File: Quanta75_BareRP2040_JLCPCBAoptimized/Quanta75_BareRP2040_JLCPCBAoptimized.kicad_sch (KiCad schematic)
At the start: 249 parts, among them J1 USB_C_Receptacle_USB2.0, J10 Conn_01x05_Socket GPIOs, J2 Conn_01x02_Socket VBUS 5V, J3 Conn_01x02_Socket 3V3, J5 Conn_01x04_Socket SWD, J6 USB_A_Receptacle_UBS2.0, J7 USB_C_Receptacle_USB2.0, J8 Conn_01x04_Socket I2C display, J9 USB_C_Receptacle_USB2.0, SW1 SW_Push, SW10 SW_Push, SW11 SW_Push, SW12 SW_Push, SW13 SW_Push, SW14 SW_Push, SW15 SW_Push, SW16 SW_Push, SW17 SW_Push, SW18 SW_Push, SW19 SW_Push, SW2 SW_Push, SW20 SW_Push, SW21 SW_Push, SW22 SW_Push, SW23 SW_Push, SW24 SW_Push, SW25 SW_Push, SW26 SW_Push, SW27 SW_Push, SW28 SW_Push, SW29 SW_Push, SW3 SW_Push, SW30 SW_Push, SW31 SW_Push, SW32 SW_Push, SW33 SW_Push, SW34 SW_Push, SW35 SW_Push, SW36 SW_Push, SW37 SW_Push, SW38 SW_Push, SW39 SW_Push, SW4 SW_Push, SW40 SW_Push, SW41 SW_Push, SW42 SW_Push, SW43 SW_Push, SW44 SW_Push, SW45 SW_Push, SW46 SW_Push, SW47 SW_Push, SW48 SW_Push, SW49 SW_Push, SW5 SW_Push, SW50 SW_Push, SW51 SW_Push, SW52 SW_Push, SW53 SW_Push, SW54 SW_Push, SW55 SW_Push, SW56 SW_Push, SW57 SW_Push, SW58 SW_Push, SW59 SW_Push, SW6 SW_Push, SW60 SW_Push, SW61 SW_Push, SW62 SW_Push, SW63 SW_Push, SW64 SW_Push, SW65 SW_Push, SW66 SW_Push, SW67 SW_Push, SW68 SW_Push, SW69 SW_Push, SW7 SW_Push, SW70 SW_Push, SW71 SW_Push, SW72 SW_Push, SW73 SW_Push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

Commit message: update pcb
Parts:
- removed D88: Amber LED, LED_THT:LED_D3.0mm_Clear, symbol Device:LED
- C12: footprint Resistor_SMD:R_0805_2012Metric_Pad1.20x1.40mm_HandSolder -> Capacitor_SMD:C_0805_2012Metric_Pad1.18x1.45mm_HandSolder
- C13, C14, C16, C17, C18, C19, C20, C21, C22: footprint Resistor_SMD:R_0603_1608Metric_Pad0.98x0.95mm_HandSolder -> Capacitor_SMD:C_0603_1608Metric_Pad1.08x0.95mm_HandSolder
- C25, C26: footprint Resistor_SMD:R_0402_1005Metric_Pad0.72x0.64mm_HandSolder -> Capacitor_SMD:C_0402_1005Metric_Pad0.74x0.62mm_HandSolder
- U1: footprint Package_DFN_QFN:QFN-56-1EP_7x7mm_P0.4mm_EP3.2x3.2mm -> Package_DFN_QFN:QFN-56-1EP_7x7mm_P0.4mm_EP3.2x3.2mm_ThermalVias
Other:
- moved on the sheet: D87
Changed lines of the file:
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@@
   (junction (at 254 101.6) (diameter 0) (color 0 0 0 0)
   )
-  (junction (at 405.13 364.49) (diameter 0) (color 0 0 0 0)
-  )
   (junction (at 87.63 309.88) (diameter 0) (color 0 0 0 0)
   )
@@
   (junction (at 171.45 101.6) (diameter 0) (color 0 0 0 0)
   )
-  (junction (at 400.05 353.06) (diameter 0) (color 0 0 0 0)
-  )
   (junction (at 204.47 170.18) (diameter 0) (color 0 0 0 0)
   )
@@
     (stroke (width 0) (type default))
   )
-  (wire (pts (xy 394.97 364.49) (xy 405.13 364.49))
+  (wire (pts (xy 400.05 364.49) (xy 407.67 364.49))
     (stroke (width 0) (type default))
   )
@@
     (stroke (width 0) (type default))
   )
-  (wire (pts (xy 394.97 353.06) (xy 400.05 353.06))
-    (stroke (width 0) (type default))
-  )
   (wire (pts (xy 99.06 144.78) (xy 99.06 147.32))
     (stroke (width 0) (type default))
@@
     (stroke (width 0) (type default))
   )
-  (wire (pts (xy 407.67 364.49) (xy 405.13 364.49))
-    (stroke (width 0) (type default))
-  )
   (wire (pts (xy 427.99 105.41) (xy 433.07 105.41))
     (stroke (width 0) (type default))
@@
     (stroke (width 0) (type default))
   )
-  (wire (pts (xy 394.97 364.49) (xy 394.97 361.95))
+  (wire (pts (xy 400.05 364.49) (xy 400.05 359.41))
     (stroke (width 0) (type default))
   )
@@
     (stroke (width 0) (type default))
   )
-  (wire (pts (xy 405.13 364.49) (xy 405.13 361.95))
-    (stroke (width 0) (type default))
-  )
   (wire (pts (xy 198.12 109.22) (xy 214.63 109.22))
     (stroke (width 0) (type default))
@@
     (stroke (width 0) (type default))
   )
-  (wire (pts (xy 394.97 353.06) (xy 394.97 354.33))
+  (wire (pts (xy 400.05 346.71) (xy 400.05 351.79))
     (stroke (width 0) (type default))
   )
@@
     (stroke (width 0) (type default))
   )
-  (wire (pts (xy 405.13 354.33) (xy 405.13 353.06))
-    (stroke (width 0) (type default))
-  )
   (wire (pts (xy 505.46 181.61) (xy 519.43 181.61))
     (stroke (width 0) (type default))
@@
     (stroke (width 0) (type default))
   )
-  (wire (pts (xy 400.05 346.71) (xy 400.05 353.06))
-    (stroke (width 0) (type default))
-  )
   (wire (pts (xy 115.57 86.36) (xy 115.57 88.9))
     (stroke (width 0) (type default))
@@
     (stroke (width 0) (type default))
   )
-  (wire (pts (xy 400.05 353.06) (xy 405.13 353.06))
-    (stroke (width 0) (type default))
-  )
   (wire (pts (xy 198.12 40.64) (xy 214.63 40.64))
     (stroke (width 0) (type default))
@@
       (effects (font (size 1.27 1.27)) (justify left))
     )
-    (property "Footprint" "Package_DFN_QFN:QFN-56-1EP_7x7mm_P0.4mm_EP3.2x3.2mm" (at 153.67 381 0)
+    (property "Footprint" "Package_DFN_QFN:QFN-56-1EP_7x7mm_P0.4mm_EP3.2x3.2mm_ThermalVias" (at 153.67 381 0)
       (effects (font (size 1.27 1.27)) hide)
     )
@@
       (effects (font (size 1.27 1.27)) (justify left))
     )
-    (property "Footprint" "Resistor_SMD:R_0603_1608Metric_Pad0.98x0.95mm_HandSolder" (at 187.96 246.38 0)
+    (property "Footprint" "Capacitor_SMD:C_0603_1608Metric_Pad1.08x0.95mm_HandSolder" (at 187.96 246.38 0)
       (effects (font (size 1.27 1.27)) hide)
     )
@@
       (effects (font (size 1.27 1.27)) (justify left))
     )
-    (property "Footprint" "Resistor_SMD:R_0603_1608Metric_Pad0.98x0.95mm_HandSolder" (at 172.72 246.38 0)
+    (property "Footprint" "Capacitor_SMD:C_0603_1608Metric_Pad1.08x0.95mm_HandSolder" (at 172.72 246.38 0)
       (effects (font (size 1.27 1.27)) hide)
     )
@@
     )
   )
-  (symbol (lib_id "Device:LED") (at 405.13 358.14 90) (unit 1)
-    (in_bom no) (on_board yes) (dnp yes)
-    (property "Reference" "D88" (at 401.32 359.41 0)
-      (effects (font (size 1.27 1.27)))
-    )
-    (property "Value" "Amber LED" (at 402.9192 358.9145 0)
-      (effects (font (size 1.27 1.27)))
-    )
-    (property "Footprint" "LED_THT:LED_D3.0mm_Clear" (at 405.13 358.14 0)
-      (effects (font (size 1.27 1.27)) hide)
-    )
-    (property "Datasheet" "~" (at 405.13 358.14 0)
-      (effects (font (size 1.27 1.27)) hide)
-    )
-    (pin "1")
-    (pin "2")
-    (instances
-      (project "Quanta75_BareRP2040_JLCPCBAoptimized"
-        (path "/0cabb2e6-4a46-4ffe-8ff7-d51fc1f6dda5"
-          (reference "D88") (unit 1)
-        )
-      )
-    )
-  )
   (symbol (lib_id "pspice:DIODE") (at 77.47 55.88 0) (unit 1)
     (in_bom yes) (on_board yes) (dnp no)
@@
       (effects (font (size 1.27 1.27)) (justify left))
     )
-    (property "Footprint" "Resistor_SMD:R_0402_1005Metric_Pad0.72x0.64mm_HandSolder" (at 135.89 261.62 0)
+    (property "Footprint" "Capacitor_SMD:C_0402_1005Metric_Pad0.74x0.62mm_HandSolder" (at 135.89 261.62 0)
       (effects (font (size 1.27 1.27)) hide)
     )
@@
       (effects (font (size 1.27 1.27)) (justify left))
     )
-    (property "Footprint" "Resistor_SMD:R_0603_1608Metric_Pad0.98x0.95mm_HandSolder" (at 110.49 246.38 0)
+    (property "Footprint" "Capacitor_SMD:C_0603_1608Metric_Pad1.08x0.95mm_HandSolder" (at 110.49 246.38 0)
       (effects (font (size 1.27 1.27)) hide)
     )
@@
       (effects (font (size 1.27 1.27)) (justify left))
     )
-    (property "Footprint" "Resistor_SMD:R_0603_1608Metric_Pad0.98x0.95mm_HandSolder" (at 69.85 248.92 0)
+    (property "Footprint" "Capacitor_SMD:C_0603_1608Metric_Pad1.08x0.95mm_HandSolder" (at 69.85 248.92 0)
       (effects (font (size 1.27 1.27)) hide)
     )
@@
       (effects (font (size 1.27 1.27)) (justify left))
     )
-    (property "Footprint" "Resistor_SMD:R_0402_1005Metric_Pad0.72x0.64mm_HandSolder" (at 149.86 261.62 0)
+    (property "Footprint" "Capacitor_SMD:C_0402_1005Metric_Pad0.74x0.62mm_HandSolder" (at 149.86 261.62 0)
       (effects (font (size 1.27 1.27)) hide)
     )
@@
       (effects (font (size 1.27 1.27)) (justify left))
     )
-    (property "Footprint" "Resistor_SMD:R_0603_1608Metric_Pad0.98x0.95mm_HandSolder" (at 120.65 246.38 0)
+    (property "Footprint" "Capacitor_SMD:C_0603_1608Metric_Pad1.08x0.95mm_HandSolder" (at 120.65 246.38 0)
       (effects (font (size 1.27 1.27)) hide)
     )
@@
       (effects (font (size 1.27 1.27)) (justify left))
     )
-    (property "Footprint" "Resistor_SMD:R_0603_1608Metric_Pad0.98x0.95mm_HandSolder" (at 165.1 246.38 0)
+    (property "Footprint" "Capacitor_SMD:C_0603_1608Metric_Pad1.08x0.95mm_HandSolder" (at 165.1 246.38 0)
       (effects (font (size 1.27 1.27)) hide)
     )
@@
     )
   )
-  (symbol (lib_id "Device:LED") (at 394.97 358.14 90) (unit 1)
+  (symbol (lib_id "Device:LED") (at 400.05 355.6 90) (unit 1)
     (in_bom no) (on_board yes) (dnp yes)
-    (property "Reference" "D87" (at 391.16 359.41 0)
+    (property "Reference" "D87" (at 396.24 356.87 0)
       (effects (font (size 1.27 1.27)))
     )
-    (property "Value" "Amber LED" (at 392.7179 359.3421 0)
+    (property "Value" "Amber LED" (at 397.7979 356.8021 0)
       (effects (font (size 1.27 1.27)))
     )
-    (property "Footprint" "LED_THT:LED_D5.0mm_Clear" (at 394.97 358.14 0)
+    (property "Footprint" "LED_THT:LED_D5.0mm_Clear" (at 400.05 355.6 0)
       (effects (font (size 1.27 1.27)) hide)
     )
-    (property "Datasheet" "~" (at 394.97 358.14 0)
+    (property "Datasheet" "~" (at 400.05 355.6 0)
       (effects (font (size 1.27 1.27)) hide)
     )
@@
       (effects (font (size 1.27 1.27)) (justify left))
     )
-    (property "Footprint" "Resistor_SMD:R_0603_1608Metric_Pad0.98x0.95mm_HandSolder" (at 195.58 246.38 0)
+    (property "Footprint" "Capacitor_SMD:C_0603_1608Metric_Pad1.08x0.95mm_HandSolder" (at 195.58 246.38 0)
       (effects (font (size 1.27 1.27)) hide)
     )
@@
       (effects (font (size 1.27 1.27)) (justify left))
     )
-    (property "Footprint" "Resistor_SMD:R_0603_1608Metric_Pad0.98x0.95mm_HandSolder" (at 180.34 246.38 0)
+    (property "Footprint" "Capacitor_SMD:C_0603_1608Metric_Pad1.08x0.95mm_HandSolder" (at 180.34 246.38 0)
       (effects (font (size 1.27 1.27)) hide)
     )
@@
       (effects (font (size 1.27 1.27)) (justify left))
     )
-    (property "Footprint" "Resistor_SMD:R_0805_2012Metric_Pad1.20x1.40mm_HandSolder" (at 81.28 248.92 0)
+    (property "Footprint" "Capacitor_SMD:C_0805_2012Metric_Pad1.18x1.45mm_HandSolder" (at 81.28 248.92 0)
       (effects (font (size 1.27 1.27)) hide)
     )
@@
       (effects (font (size 1.27 1.27)) (justify left))
     )
-    (property "Footprint" "Resistor_SMD:R_0603_1608Metric_Pad0.98x0.95mm_HandSolder" (at 49.53 248.92 0)
+    (property "Footprint" "Capacitor_SMD:C_0603_1608Metric_Pad1.08x0.95mm_HandSolder" (at 49.53 248.92 0)
       (effects (font (size 1.27 1.27)) hide)
     )

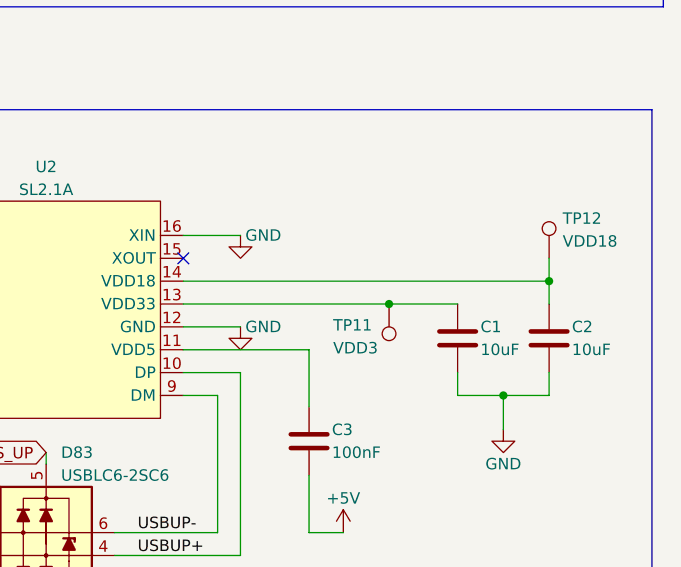
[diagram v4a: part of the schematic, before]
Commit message: finalized rp2040 version placements
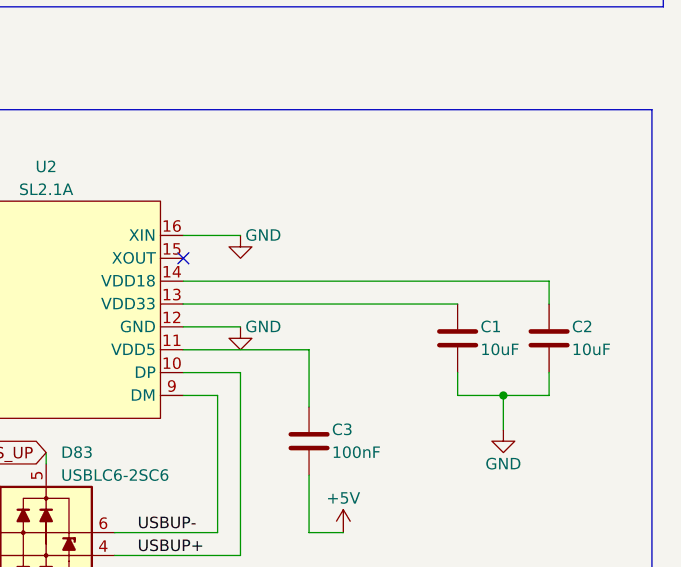
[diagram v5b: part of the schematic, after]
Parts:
- removed TP11: VDD3, TestPoint:TestPoint_Pad_D1.5mm, symbol Connector:TestPoint
- removed TP12: VDD18, TestPoint:TestPoint_Pad_D1.5mm, symbol Connector:TestPoint
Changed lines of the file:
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@@
   (junction (at 247.65 40.64) (diameter 0) (color 0 0 0 0)
   )
-  (junction (at 535.94 153.67) (diameter 0) (color 0 0 0 0)
-  )
   (junction (at 105.41 147.32) (diameter 0) (color 0 0 0 0)
   )
@@
   (junction (at 69.85 245.11) (diameter 0) (color 0 0 0 0)
   )
-  (junction (at 553.72 151.13) (diameter 0) (color 0 0 0 0)
-  )
   (junction (at 172.72 241.3) (diameter 0) (color 0 0 0 0)
   )
@@
     (stroke (width 0) (type default))
   )
-  (wire (pts (xy 543.56 153.67) (xy 535.94 153.67))
-    (stroke (width 0) (type default))
-  )
   (wire (pts (xy 237.49 78.74) (xy 237.49 101.6))
     (stroke (width 0) (type default))
@@
     (stroke (width 0) (type default))
   )
-  (wire (pts (xy 513.08 153.67) (xy 535.94 153.67))
+  (wire (pts (xy 513.08 153.67) (xy 543.56 153.67))
     (stroke (width 0) (type default))
   )
@@
     (stroke (width 0) (type default))
   )
-  (wire (pts (xy 553.72 148.59) (xy 553.72 151.13))
-    (stroke (width 0) (type default))
-  )
   (wire (pts (xy 412.75 148.59) (xy 430.53 148.59))
     (stroke (width 0) (type default))
@@
     )
   )
-  (symbol (lib_id "Connector:TestPoint") (at 553.72 148.59 0) (unit 1)
-    (in_bom yes) (on_board yes) (dnp no)
-    (property "Reference" "TP12" (at 555.2305 144.1697 0)
-      (effects (font (size 1.27 1.27)) (justify left))
-    )
-    (property "Value" "VDD18" (at 555.2305 146.7097 0)
-      (effects (font (size 1.27 1.27)) (justify left))
-    )
-    (property "Footprint" "TestPoint:TestPoint_Pad_D1.5mm" (at 558.8 148.59 0)
-      (effects (font (size 1.27 1.27)) hide)
-    )
-    (property "Datasheet" "~" (at 558.8 148.59 0)
-      (effects (font (size 1.27 1.27)) hide)
-    )
-    (pin "1")
-    (instances
-      (project "Quanta75_BareRP2040_JLCPCBAoptimized"
-        (path "/0cabb2e6-4a46-4ffe-8ff7-d51fc1f6dda5"
-          (reference "TP12") (unit 1)
-        )
-      )
-    )
-  )
   (symbol (lib_id "power:+3V3") (at 86.36 242.57 0) (unit 1)
     (in_bom yes) (on_board yes) (dnp no) (fields_autoplaced)
@@
         )
       )
-    )
-  )
-  (symbol (lib_id "Connector:TestPoint") (at 535.94 153.67 180) (unit 1)
-    (in_bom yes) (on_board yes) (dnp no)
-    (property "Reference" "TP11" (at 529.7257 156.0324 0)
-      (effects (font (size 1.27 1.27)) (justify right))
-    )
-    (property "Value" "VDD3" (at 529.7257 158.5724 0)
-      (effects (font (size 1.27 1.27)) (justify right))
-    )
-    (property "Footprint" "TestPoint:TestPoint_Pad_D1.5mm" (at 530.86 153.67 0)
-      (effects (font (size 1.27 1.27)) hide)
-    )
-    (property "Datasheet" "~" (at 530.86 153.67 0)
-      (effects (font (size 1.27 1.27)) hide)
-    )
-    (pin "1")
-    (instances
-      (project "Quanta75_BareRP2040_JLCPCBAoptimized"
-        (path "/0cabb2e6-4a46-4ffe-8ff7-d51fc1f6dda5"
-          (reference "TP11") (unit 1)
-        )
-      )
